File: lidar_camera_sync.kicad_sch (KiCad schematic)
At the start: 0 parts

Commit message: [New]: 完成MCU部分电路原理图\JIRA-ID: N/A\完成MCU部分原理图绘制以及部分Power部分原理图绘制
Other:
- added sheet MCU (MCU.kicad_sch)
- added sheet Peripheral (Peripheral.kicad_sch)
- added sheet Power (Power.kicad_sch)
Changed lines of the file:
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@@
 	(generator_version "9.0")
 	(paper "A4")
+	(sheet
+		(at 129.794 36.322)
+		(size 61.976 41.91)
+		(exclude_from_sim no)
+		(in_bom yes)
+		(on_board yes)
+		(dnp no)
+		(fields_autoplaced yes)
+		(stroke
+			(width 0.1524)
+			(type solid)
+		)
+		(fill
+			(color 255 255 194 1.0000)
+		)
+		(property "Sheetname" "Power"
+			(at 129.794 35.6104 0)
+			(effects
+				(font
+					(size 1.27 1.27)
+				)
+				(justify left bottom)
+			)
+		)
+		(property "Sheetfile" "Power.kicad_sch"
+			(at 129.794 78.8166 0)
+			(effects
+				(font
+					(size 1.27 1.27)
+				)
+				(justify left top)
+			)
+		)
+		(instances
+			(project "lidar_camera_sync"
+				(path "/4d41fa76-12ab-4867-bf30-96d46704f2ab"
+					(page "3")
+				)
+			)
+		)
+	)
+	(sheet
+		(at 47.244 36.068)
+		(size 56.134 42.164)
+		(exclude_from_sim no)
+		(in_bom yes)
+		(on_board yes)
+		(dnp no)
+		(fields_autoplaced yes)
+		(stroke
+			(width 0.1524)
+			(type solid)
+		)
+		(fill
+			(color 255 255 194 1.0000)
+		)
+		(property "Sheetname" "MCU"
+			(at 47.244 35.3564 0)
+			(effects
+				(font
+					(size 1.27 1.27)
+				)
+				(justify left bottom)
+			)
+		)
+		(property "Sheetfile" "MCU.kicad_sch"
+			(at 47.244 78.8166 0)
+			(effects
+				(font
+					(size 1.27 1.27)
+				)
+				(justify left top)
+			)
+		)
+		(pin "GND" passive
+			(at 103.378 58.42 0)
+			(effects
+				(font
+					(size 1.27 1.27)
+				)
+				(justify right)
+			)
+		)
+		(pin "PWM_CH1" output
+			(at 93.98 78.232 270)
+			(effects
+				(font
+					(size 1.27 1.27)
+				)
+				(justify left)
+			)
+		)
+		(pin "PWM_CH2" output
+			(at 90.17 78.232 270)
+			(effects
+				(font
+					(size 1.27 1.27)
+				)
+				(justify left)
+			)
+		)
+		(pin "STATE_LED" output
+			(at 86.36 78.232 270)
+			(effects
+				(font
+					(size 1.27 1.27)
+				)
+				(justify left)
+			)
+		)
+		(pin "USART2_RXD" input
+			(at 78.74 78.232 270)
+			(effects
+				(font
+					(size 1.27 1.27)
+				)
+				(justify left)
+			)
+		)
+		(pin "USART2_TXD" output
+			(at 74.93 78.232 270)
+			(effects
+				(font
+					(size 1.27 1.27)
+				)
+				(justify left)
+			)
+		)
+		(pin "VCC_3V3" input
+			(at 103.378 54.61 0)
+			(effects
+				(font
+					(size 1.27 1.27)
+				)
+				(justify right)
+			)
+		)
+		(pin "VCC_5V0" input
+			(at 103.378 50.8 0)
+			(effects
+				(font
+					(size 1.27 1.27)
+				)
+				(justify right)
+			)
+		)
+		(instances
+			(project "lidar_camera_sync"
+				(path "/4d41fa76-12ab-4867-bf30-96d46704f2ab"
+					(page "2")
+				)
+			)
+		)
+	)
+	(sheet
+		(at 47.498 91.44)
+		(size 55.88 41.148)
+		(exclude_from_sim no)
+		(in_bom yes)
+		(on_board yes)
+		(dnp no)
+		(fields_autoplaced yes)
+		(stroke
+			(width 0.1524)
+			(type solid)
+		)
+		(fill
+			(color 255 255 194 1.0000)
+		)
+		(property "Sheetname" "Peripheral"
+			(at 47.498 90.7284 0)
+			(effects
+				(font
+					(size 1.27 1.27)
+				)
+				(justify left bottom)
+			)
+		)
+		(property "Sheetfile" "Peripheral.kicad_sch"
+			(at 47.498 133.1726 0)
+			(effects
+				(font
+					(size 1.27 1.27)
+				)
+				(justify left top)
+			)
+		)
+		(instances
+			(project "lidar_camera_sync"
+				(path "/4d41fa76-12ab-4867-bf30-96d46704f2ab"
+					(page "4")
+				)
+			)
+		)
+	)
 	(sheet_instances
 		(path "/"

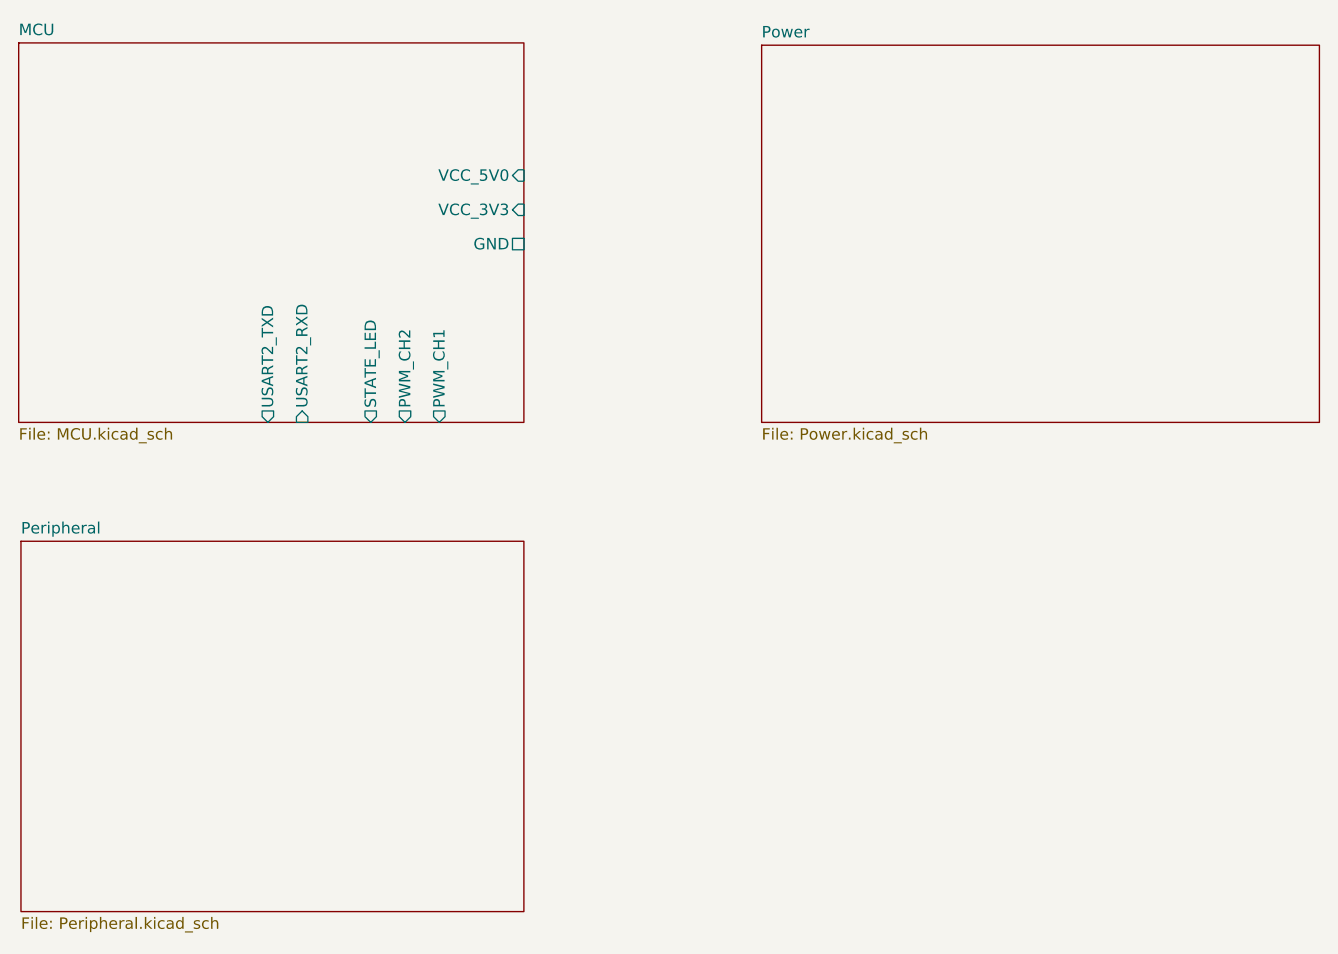
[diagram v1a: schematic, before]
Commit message: [New]: 完成整个原理图绘制和ERC检查
JIRA-ID: N/A

完成整个原理图绘制和ERC检查
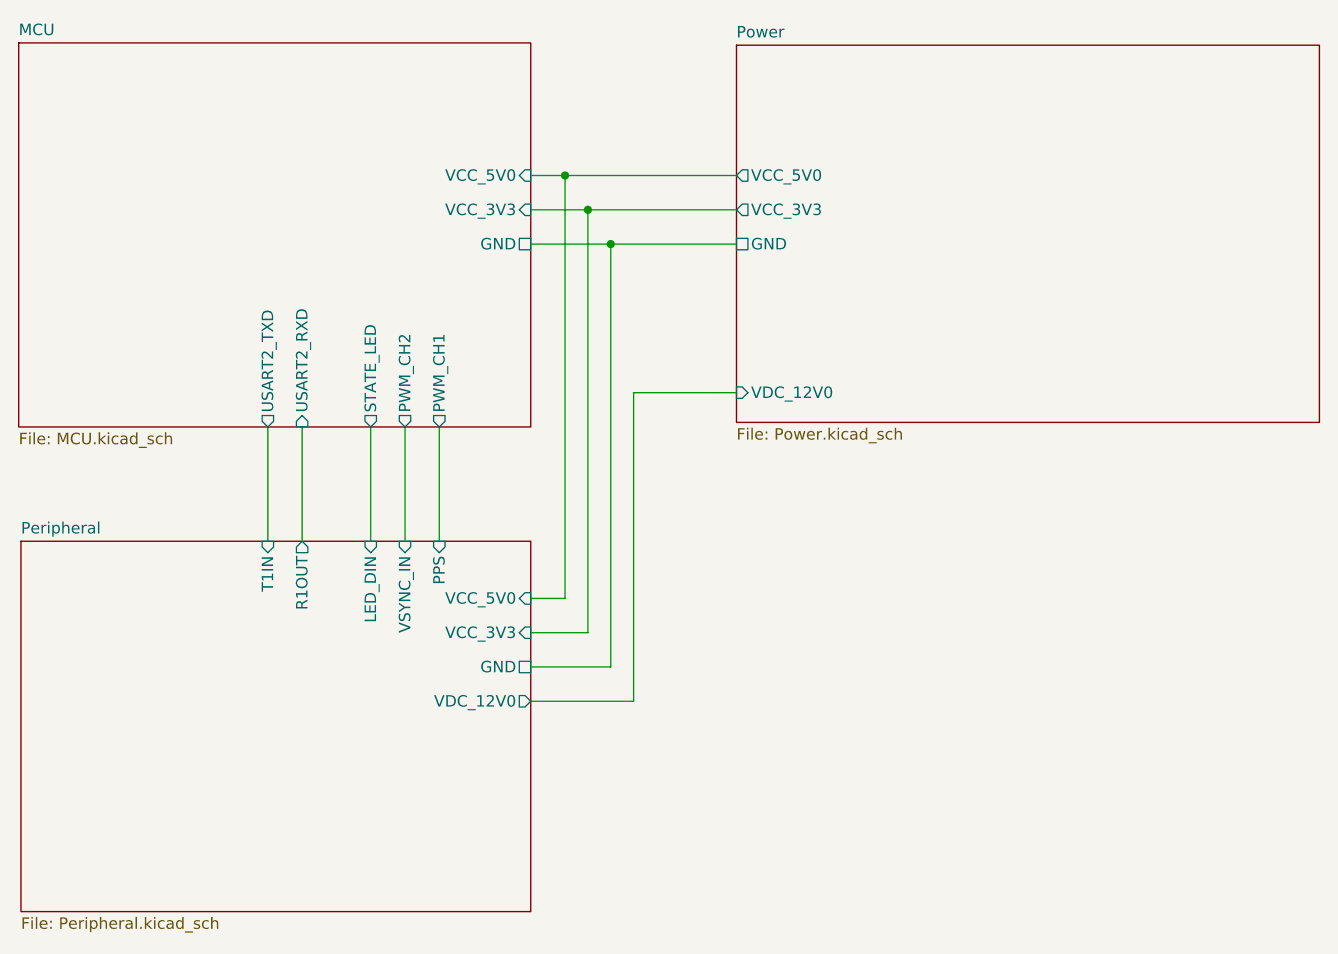
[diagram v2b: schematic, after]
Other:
- sheet Peripheral ports: added GND, LED_DIN, PPS, R1OUT, T1IN, VCC_3V3, VCC_5V0, VDC_12V0, VSYNC_IN; removed none
- sheet Power ports: added GND, VCC_3V3, VCC_5V0, VDC_12V0; removed none

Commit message: [Fix]: 添加雷达供电隔离
JIRA-ID: N/A

添加雷达信号隔离电路，检查原理图错误，新增原理图符号
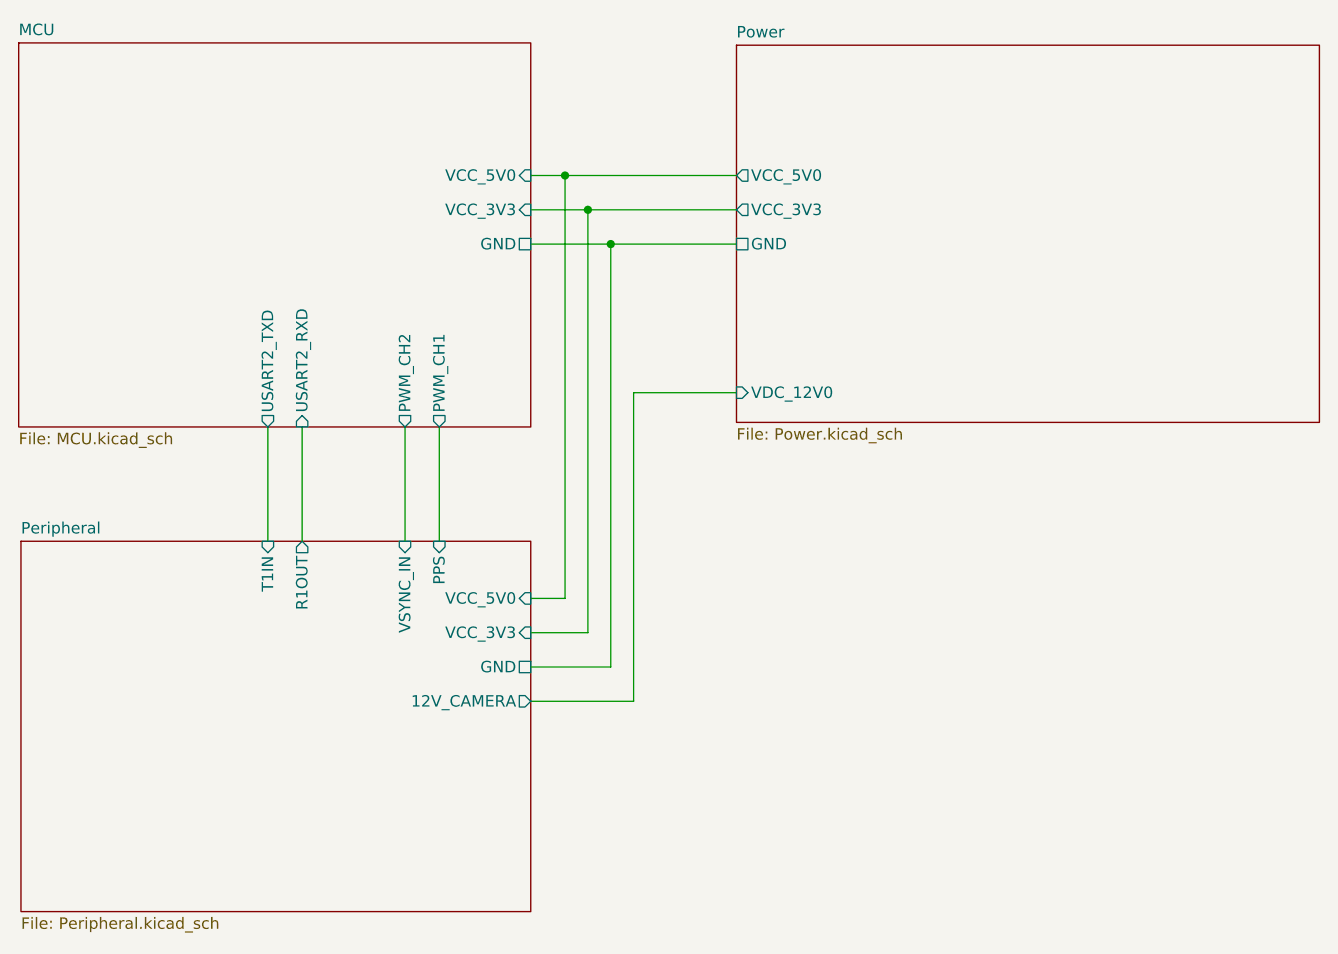
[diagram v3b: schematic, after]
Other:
- sheet MCU ports: added none; removed STATE_LED
- sheet Peripheral ports: added 12V_CAMERA; removed LED_DIN, VDC_12V0
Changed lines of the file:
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@@
-	(wire
-		(pts
-			(xy 86.36 78.74) (xy 86.36 91.44)
-		)
-		(stroke
-			(width 0)
-			(type default)
-		)
-	)
 	(wire
 		(pts
@@
 			)
 		)
-		(pin "STATE_LED" output
-			(at 86.36 78.74 270)
-			(effects
-				(font
-					(size 1.27 1.27)
-				)
-				(justify left)
-			)
-		)
 		(pin "USART2_RXD" input
 			(at 78.74 78.74 270)
@@
 			)
 		)
-		(pin "LED_DIN" input
-			(at 86.36 91.44 90)
-			(effects
-				(font
-					(size 1.27 1.27)
-				)
-				(justify right)
-			)
-		)
 		(pin "R1OUT" output
 			(at 78.74 91.44 90)
@@
 			)
 		)
-		(pin "VDC_12V0" output
-			(at 104.14 109.22 0)
-			(effects
-				(font
-					(size 1.27 1.27)
-				)
-				(justify right)
-			)
-		)
 		(pin "GND" passive
 			(at 104.14 105.41 0)
@@
 			(effects
 				(font
+					(size 1.27 1.27)
+				)
+				(justify right)
+			)
+		)
+		(pin "12V_CAMERA" output
+			(at 104.14 109.22 0)
+			(effects
+				(font

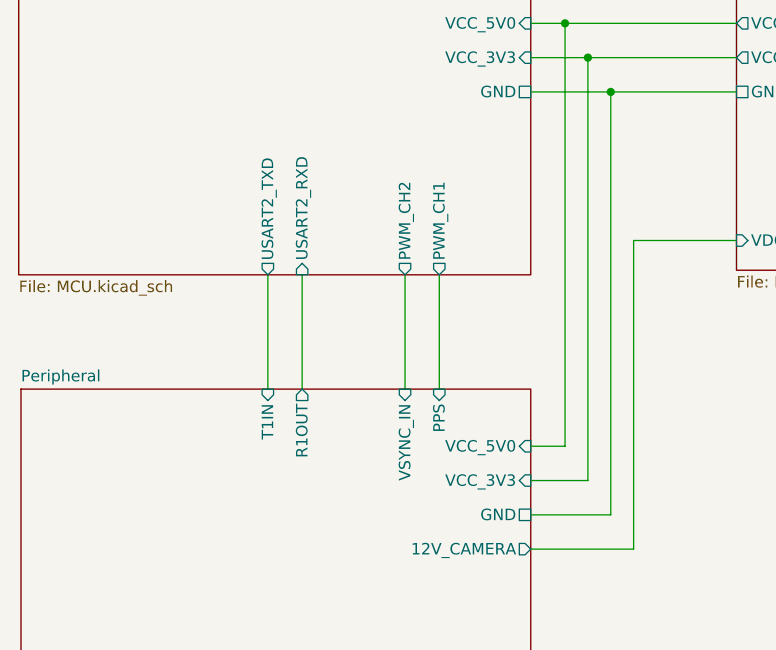
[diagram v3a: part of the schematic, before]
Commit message: [Modify]: 添加输入输出去耦电容以及WS2812B灯珠
JIRA-ID: N/A

添加输入输出去耦电容以及WS2812B灯珠
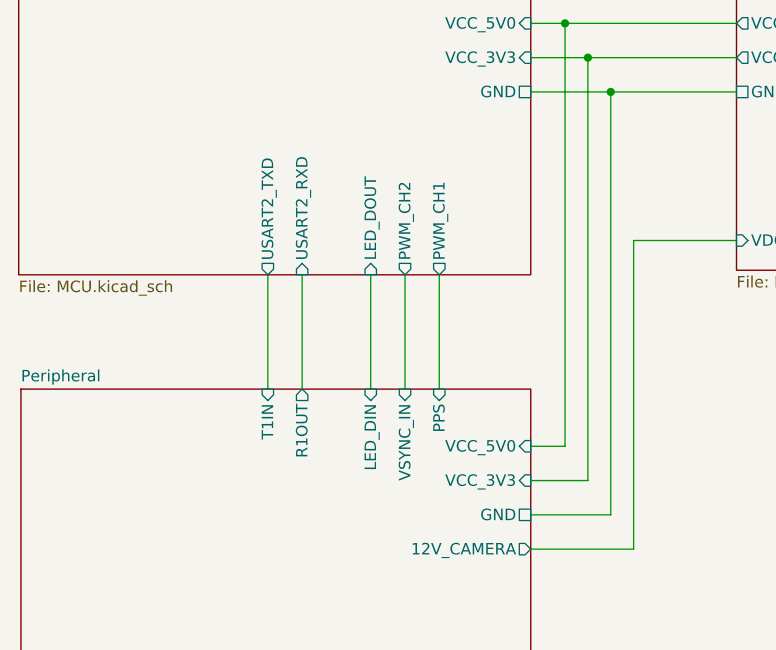
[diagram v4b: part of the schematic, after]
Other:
- sheet MCU ports: added LED_DOUT; removed none
- sheet Peripheral ports: added LED_DIN; removed none
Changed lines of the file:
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@@
+	(wire
+		(pts
+			(xy 86.36 78.74) (xy 86.36 91.44)
+		)
+		(stroke
+			(width 0)
+			(type default)
+		)
+	)
 	(wire
 		(pts
@@
 			)
 		)
+		(pin "LED_DOUT" input
+			(at 86.36 78.74 270)
+			(effects
+				(font
+					(size 1.27 1.27)
+				)
+				(justify left)
+			)
+		)
 		(instances
 			(project "lidar_camera_sync"
@@
 			(effects
 				(font
+					(size 1.27 1.27)
+				)
+				(justify right)
+			)
+		)
+		(pin "LED_DIN" input
+			(at 86.36 91.44 90)
+			(effects
+				(font
